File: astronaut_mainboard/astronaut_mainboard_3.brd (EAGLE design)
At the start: 69.5 x 52.1 mm, 23 parts, among them IC1 ADUM1250, IC2 741G3157DBVR, IC3 741G3157DBVR, J10 HF Comm, J6 Ext 5V, J7 UI, J8 Arduino (DWM), J9 GNSS, Q1 BSS138, Q3 BSS138

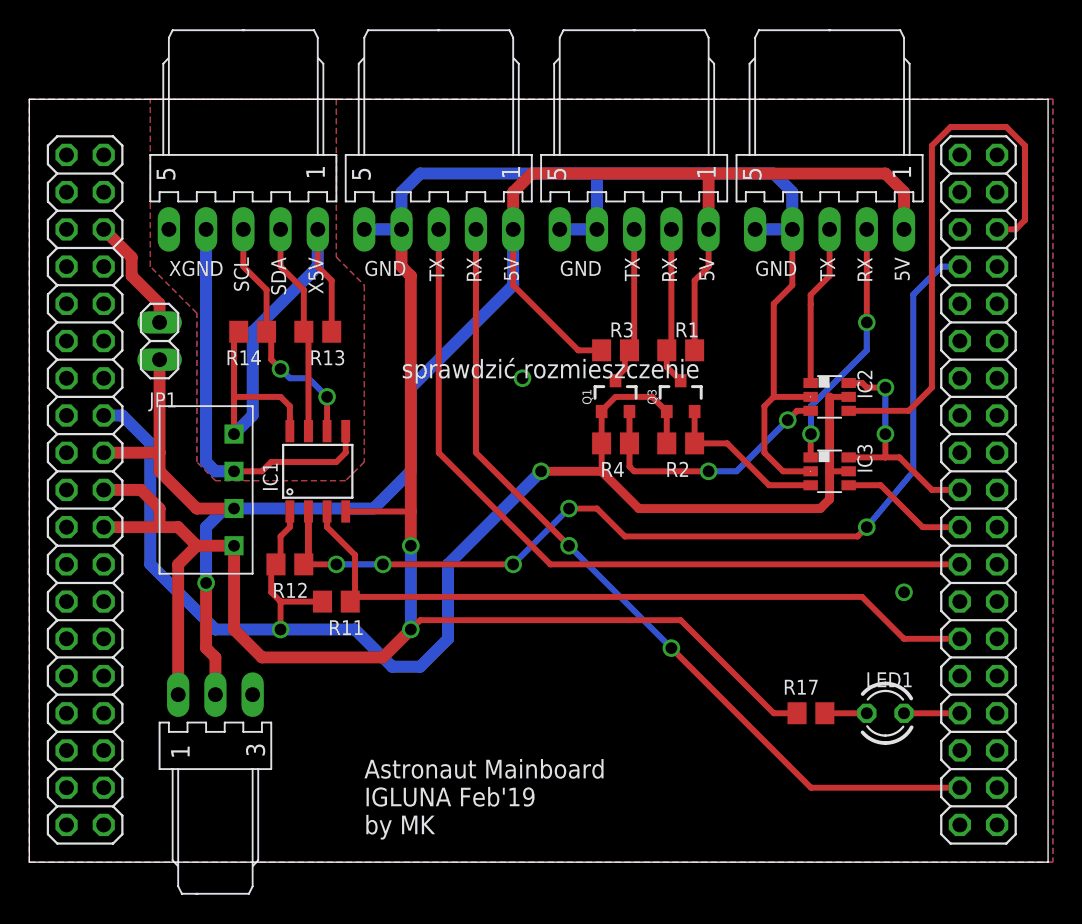
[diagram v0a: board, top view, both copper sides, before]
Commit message: updated lib, corrected boards (after printing)
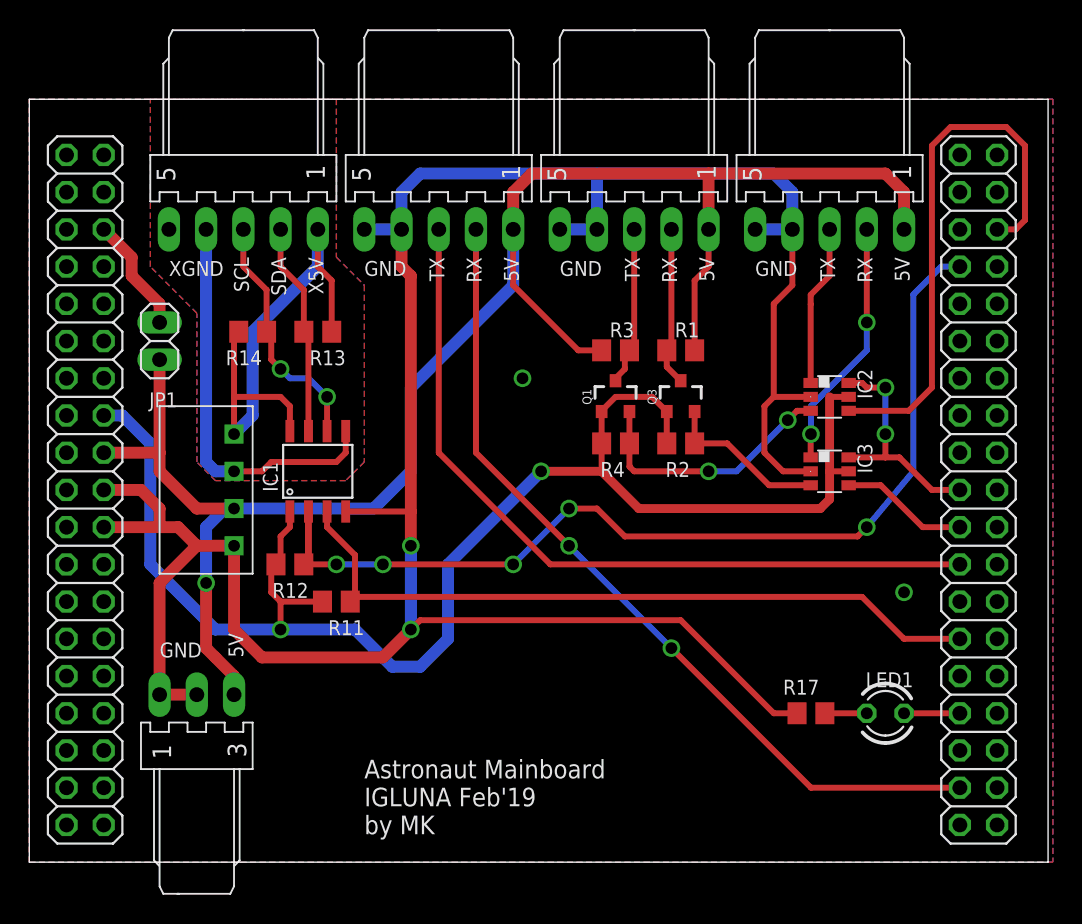
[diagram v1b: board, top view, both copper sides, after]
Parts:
- moved J6 1.27 mm to (12.7, 11.4)
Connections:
- net +5V: no longer J6.2
- net GND: now also J6.2
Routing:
- net GND: track 172.8 -> 175.9 mm
- net +5V: track 121.2 -> 121.7 mm
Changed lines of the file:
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@@
 IGLUNA Feb'19
 by MK</text>
+<text x="15.875" y="13.97" size="1.016" layer="25" rot="R90">5V</text>
+<text x="10.16" y="13.97" size="1.016" layer="25">GND</text>
 </plain>
 <attributes>
@@
 <attribute name="VALUE" x="6.985" y="38.1" size="1.27" layer="27" rot="R270"/>
 </element>
-<element name="J6" library="EP_molex_6410_7395" package="7395-03" value="Ext 5V" x="13.97" y="11.43" smashed="yes" rot="R180">
-<attribute name="VALUE" x="18.6421" y="8.9901" size="1.27" layer="27" ratio="10" rot="R270"/>
+<element name="J6" library="EP_molex_6410_7395" package="7395-03" value="Ext 5V" x="12.7" y="11.43" smashed="yes" rot="R180">
+<attribute name="VALUE" x="17.3721" y="8.9901" size="1.27" layer="27" ratio="10" rot="R270"/>
 </element>
 <element name="J7" library="EP_molex_6410_7395" package="7395-05" value="UI" x="15.875" y="43.18" smashed="yes">
@@
 <contactref element="IC2" pad="2"/>
 <contactref element="R17" pad="1"/>
-<contactref element="U$3" pad="19"/>
-<contactref element="U$3" pad="8"/>
 <contactref element="U$3" pad="20"/>
 <contactref element="U$3" pad="22"/>
-<contactref element="U$3" pad="47"/>
-<contactref element="U$3" pad="58"/>
 <wire x1="6.35" y1="22.86" x2="10.16" y2="22.86" width="0.8128" layer="1"/>
 <wire x1="53.34" y1="43.18" x2="53.34" y2="45.72" width="0.8128" layer="16"/>
@@
 <contactref element="J8" pad="5"/>
 <contactref element="J6" pad="1"/>
-<wire x1="11.43" y1="11.43" x2="11.43" y2="20.32" width="0.8128" layer="1"/>
-<wire x1="11.43" y1="20.32" x2="12.7" y2="21.59" width="0.8128" layer="1"/>
+<wire x1="10.16" y1="11.43" x2="10.16" y2="19.05" width="0.8128" layer="1"/>
+<wire x1="10.16" y1="19.05" x2="12.7" y2="21.59" width="0.8128" layer="1"/>
 <wire x1="26.67" y1="43.18" x2="24.13" y2="43.18" width="0.8128" layer="16"/>
 <wire x1="37.465" y1="43.18" x2="40.005" y2="43.18" width="0.8128" layer="16"/>
@@
 <via x="34.925" y="33.02" extent="1-16" drill="0.8"/>
 <via x="60.96" y="18.415" extent="1-16" drill="0.8"/>
+<contactref element="U$3" pad="19"/>
+<contactref element="U$3" pad="8"/>
+<contactref element="U$3" pad="47"/>
+<contactref element="U$3" pad="58"/>
+<contactref element="J6" pad="2"/>
+<wire x1="10.16" y1="11.43" x2="12.7" y2="11.43" width="0.8128" layer="1"/>
 </signal>
 <signal name="VIN">
@@
 <contactref element="J10" pad="1"/>
 <contactref element="J8" pad="1"/>
-<contactref element="J6" pad="2"/>
 <contactref element="J6" pad="3"/>
 <wire x1="12.7" y1="24.13" x2="10.16" y2="26.67" width="0.8128" layer="1"/>
@@
 <wire x1="13.335" y1="19.05" x2="13.335" y2="14.605" width="0.8128" layer="1"/>
 <wire x1="13.335" y1="14.605" x2="13.97" y2="13.97" width="0.8128" layer="1"/>
-<wire x1="13.97" y1="13.97" x2="13.97" y2="11.43" width="0.8128" layer="1"/>
 <via x="13.335" y="19.05" extent="1-16" drill="0.8"/>
 <wire x1="27.305" y1="32.385" x2="34.29" y2="39.37" width="0.8128" layer="16"/>
 <wire x1="34.29" y1="39.37" x2="34.29" y2="43.18" width="0.8128" layer="16"/>
-<wire x1="13.97" y1="11.43" x2="16.51" y2="11.43" width="0" layer="19" extent="1-1"/>
+<wire x1="13.97" y1="13.97" x2="15.24" y2="12.7" width="0.8128" layer="1"/>
+<wire x1="15.24" y1="12.7" x2="15.24" y2="11.43" width="0.8128" layer="1"/>
 </signal>
 <signal name="VCC">

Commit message: verified, ready to production
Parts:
- LED1: device led:LED3MM -> led:SML1206
- R17: value 470 -> 100
- turned LED1 to 0 degrees
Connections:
- net N$3: now also LED1.C; no longer LED1.K

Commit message: final, after another review
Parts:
- moved JP1 0.63 mm to (9.53, 35.6)
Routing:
- net +5V: track 121.7 -> 120.9 mm

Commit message: really final projects, added gerber files
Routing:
- net GND: vias 4 -> 5
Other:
- board text added: "."
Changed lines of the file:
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@@
 <layer number="19" name="Unrouted" color="6" fill="1" visible="yes" active="yes"/>
 <layer number="20" name="Dimension" color="15" fill="1" visible="yes" active="yes"/>
-<layer number="21" name="tPlace" color="7" fill="1" visible="yes" active="yes"/>
+<layer number="21" name="tPlace" color="7" fill="1" visible="no" active="yes"/>
 <layer number="22" name="bPlace" color="7" fill="1" visible="yes" active="yes"/>
 <layer number="23" name="tOrigins" color="15" fill="1" visible="yes" active="yes"/>
@@
 <layer number="27" name="tValues" color="7" fill="1" visible="yes" active="yes"/>
 <layer number="28" name="bValues" color="7" fill="1" visible="yes" active="yes"/>
-<layer number="29" name="tStop" color="7" fill="3" visible="no" active="yes"/>
-<layer number="30" name="bStop" color="7" fill="6" visible="no" active="yes"/>
-<layer number="31" name="tCream" color="7" fill="4" visible="no" active="yes"/>
-<layer number="32" name="bCream" color="7" fill="5" visible="no" active="yes"/>
-<layer number="33" name="tFinish" color="6" fill="3" visible="no" active="yes"/>
-<layer number="34" name="bFinish" color="6" fill="6" visible="no" active="yes"/>
-<layer number="35" name="tGlue" color="7" fill="4" visible="no" active="yes"/>
-<layer number="36" name="bGlue" color="7" fill="5" visible="no" active="yes"/>
-<layer number="37" name="tTest" color="7" fill="1" visible="no" active="yes"/>
-<layer number="38" name="bTest" color="7" fill="1" visible="no" active="yes"/>
+<layer number="29" name="tStop" color="7" fill="3" visible="yes" active="yes"/>
+<layer number="30" name="bStop" color="7" fill="6" visible="yes" active="yes"/>
+<layer number="31" name="tCream" color="7" fill="4" visible="yes" active="yes"/>
+<layer number="32" name="bCream" color="7" fill="5" visible="yes" active="yes"/>
+<layer number="33" name="tFinish" color="6" fill="3" visible="yes" active="yes"/>
+<layer number="34" name="bFinish" color="6" fill="6" visible="yes" active="yes"/>
+<layer number="35" name="tGlue" color="7" fill="4" visible="yes" active="yes"/>
+<layer number="36" name="bGlue" color="7" fill="5" visible="yes" active="yes"/>
+<layer number="37" name="tTest" color="7" fill="1" visible="yes" active="yes"/>
+<layer number="38" name="bTest" color="7" fill="1" visible="yes" active="yes"/>
 <layer number="39" name="tKeepout" color="4" fill="11" visible="yes" active="yes"/>
 <layer number="40" name="bKeepout" color="1" fill="11" visible="yes" active="yes"/>
@@
 <layer number="42" name="bRestrict" color="1" fill="10" visible="yes" active="yes"/>
 <layer number="43" name="vRestrict" color="2" fill="10" visible="yes" active="yes"/>
-<layer number="44" name="Drills" color="7" fill="1" visible="no" active="yes"/>
-<layer number="45" name="Holes" color="7" fill="1" visible="no" active="yes"/>
-<layer number="46" name="Milling" color="3" fill="1" visible="no" active="yes"/>
-<layer number="47" name="Measures" color="7" fill="1" visible="no" active="yes"/>
+<layer number="44" name="Drills" color="7" fill="1" visible="yes" active="yes"/>
+<layer number="45" name="Holes" color="7" fill="1" visible="yes" active="yes"/>
+<layer number="46" name="Milling" color="3" fill="1" visible="yes" active="yes"/>
+<layer number="47" name="Measures" color="7" fill="1" visible="yes" active="yes"/>
 <layer number="48" name="Document" color="7" fill="1" visible="yes" active="yes"/>
 <layer number="49" name="Reference" color="7" fill="1" visible="yes" active="yes"/>
@@
 <layer number="112" name="tSilk" color="7" fill="1" visible="yes" active="yes"/>
 <layer number="113" name="IDFDebug" color="4" fill="1" visible="yes" active="yes"/>
-<layer number="114" name="Badge_Outline" color="7" fill="1" visible="no" active="yes"/>
-<layer number="115" name="ReferenceISLANDS" color="7" fill="1" visible="no" active="yes"/>
+<layer number="114" name="Badge_Outline" color="7" fill="1" visible="yes" active="yes"/>
+<layer number="115" name="ReferenceISLANDS" color="7" fill="1" visible="yes" active="yes"/>
 <layer number="116" name="Patch_BOT" color="9" fill="4" visible="yes" active="yes"/>
-<layer number="118" name="Rect_Pads" color="7" fill="1" visible="no" active="yes"/>
+<layer number="118" name="Rect_Pads" color="7" fill="1" visible="yes" active="yes"/>
 <layer number="121" name="_tsilk" color="7" fill="1" visible="yes" active="yes"/>
 <layer number="122" name="_bsilk" color="7" fill="1" visible="yes" active="yes"/>
@@
 <text x="15.875" y="13.97" size="1.27" layer="25" font="vector" ratio="15" rot="R90">5V</text>
 <text x="10.16" y="13.97" size="1.27" layer="25" font="vector" ratio="15">GND</text>
+<text x="19.304" y="25.146" size="1.27" layer="25" font="vector" ratio="15" rot="R90">.</text>
+<text x="54.356" y="33.274" size="1.27" layer="25" font="vector" ratio="15" rot="R270">.</text>
+<text x="54.356" y="28.194" size="1.27" layer="25" font="vector" ratio="15" rot="R270">.</text>
+<text x="58.166" y="11.049" size="1.27" layer="25" font="vector" ratio="15" rot="R270">.</text>
 </plain>
 <attributes>
@@
 </class>
 </classes>
-<designrules name="default *">
+<designrules name="jlcpcb_rules">
 <description language="de">&lt;b&gt;EAGLE Design Rules&lt;/b&gt;
 &lt;p&gt;
@@
 <param name="mtCopper" value="0.035mm 0.035mm 0.035mm 0.035mm 0.035mm 0.035mm 0.035mm 0.035mm 0.035mm 0.035mm 0.035mm 0.035mm 0.035mm 0.035mm 0.035mm 0.035mm"/>
 <param name="mtIsolate" value="1.5mm 0.15mm 0.2mm 0.15mm 0.2mm 0.15mm 0.2mm 0.15mm 0.2mm 0.15mm 0.2mm 0.15mm 0.2mm 0.15mm 0.2mm"/>
-<param name="mdWireWire" value="12mil"/>
-<param name="mdWirePad" value="12mil"/>
-<param name="mdWireVia" value="12mil"/>
-<param name="mdPadPad" value="10mil"/>
-<param name="mdPadVia" value="12mil"/>
-<param name="mdViaVia" value="12mil"/>
-<param name="mdSmdPad" value="10mil"/>
-<param name="mdSmdVia" value="10mil"/>
-<param name="mdSmdSmd" value="10mil"/>
-<param name="mdViaViaSameLayer" value="8mil"/>
+<param name="mdWireWire" value="5mil"/>
+<param name="mdWirePad" value="5mil"/>
+<param name="mdWireVia" value="5mil"/>
+<param name="mdPadPad" value="5mil"/>
+<param name="mdPadVia" value="5mil"/>
+<param name="mdViaVia" value="5mil"/>
+<param name="mdSmdPad" value="5mil"/>
+<param name="mdSmdVia" value="5mil"/>
+<param name="mdSmdSmd" value="5mil"/>
+<param name="mdViaViaSameLayer" value="6mil"/>
 <param name="mnLayersViaInSmd" value="2"/>
-<param name="mdCopperDimension" value="20mil"/>
+<param name="mdCopperDimension" value="0.2mm"/>
 <param name="mdDrill" value="12mil"/>
 <param name="mdSmdStop" value="0mil"/>
-<param name="msWidth" value="12mil"/>
-<param name="msDrill" value="24mil"/>
+<param name="msWidth" value="5mil"/>
+<param name="msDrill" value="0.2mm"/>
 <param name="msMicroVia" value="9.99mm"/>
 <param name="msBlindViaRatio" value="0.5"/>
@@
 <param name="rvMicroViaOuter" value="0.25"/>
 <param name="rvMicroViaInner" value="0.25"/>
-<param name="rlMinPadTop" value="10mil"/>
+<param name="rlMinPadTop" value="3mil"/>
 <param name="rlMaxPadTop" value="20mil"/>
 <param name="rlMinPadInner" value="10mil"/>
@@
 <param name="rlMinPadBottom" value="10mil"/>
 <param name="rlMaxPadBottom" value="20mil"/>
-<param name="rlMinViaOuter" value="8mil"/>
+<param name="rlMinViaOuter" value="3mil"/>
 <param name="rlMaxViaOuter" value="20mil"/>
 <param name="rlMinViaInner" value="8mil"/>
@@
 <param name="srMinRoundness" value="0mil"/>
 <param name="srMaxRoundness" value="0mil"/>
-<param name="slThermalIsolate" value="12mil"/>
+<param name="slThermalIsolate" value="10mil"/>
 <param name="slThermalsForVias" value="0"/>
 <param name="dpMaxLengthDifference" value="10mm"/>
@@
 <contactref element="J6" pad="2"/>
 <wire x1="10.16" y1="11.43" x2="12.7" y2="11.43" width="0.8128" layer="1"/>
+<via x="11.43" y="21.59" extent="1-16" drill="0.8"/>
 </signal>
 <signal name="VIN">

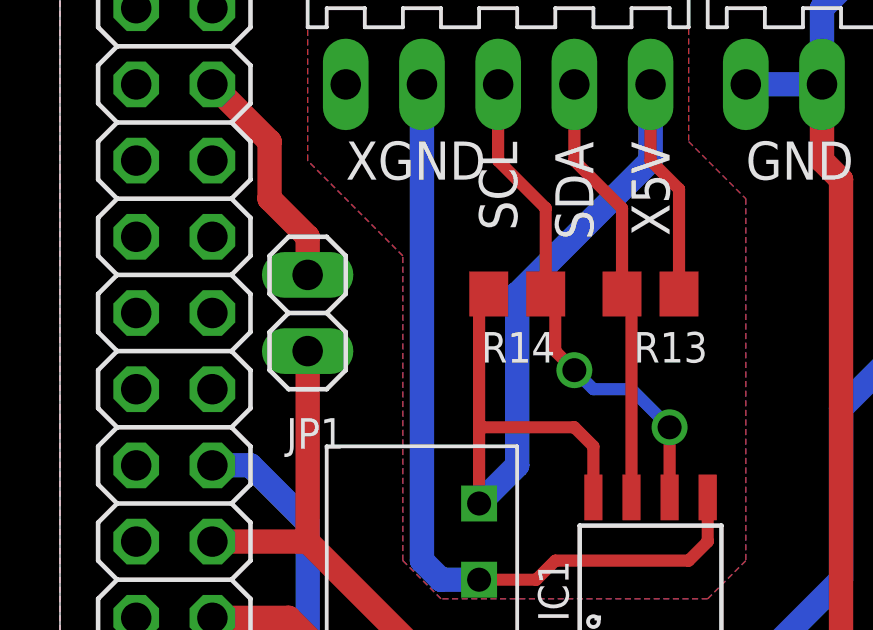
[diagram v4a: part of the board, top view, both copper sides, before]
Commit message: corrected gerbers, cleaned schematics, added documnetation
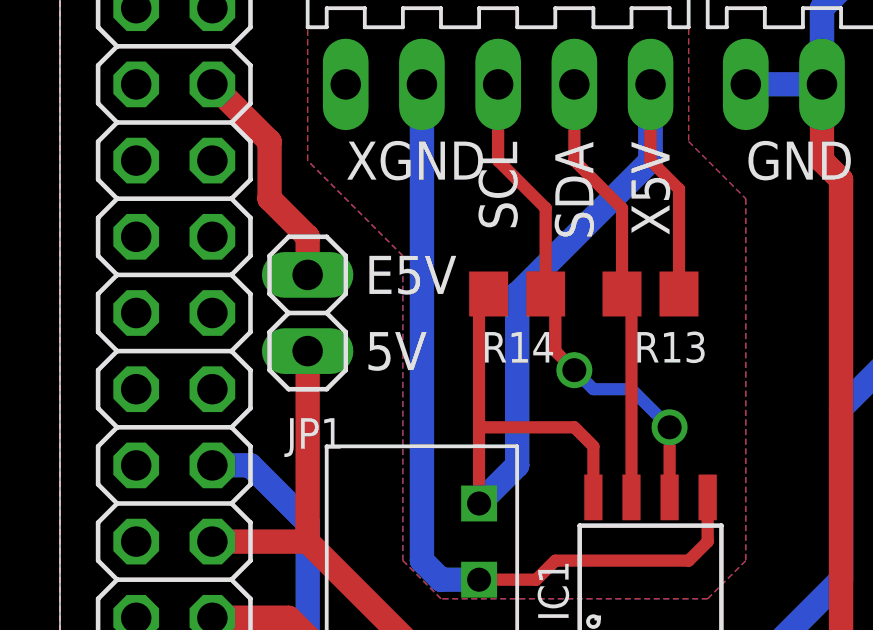
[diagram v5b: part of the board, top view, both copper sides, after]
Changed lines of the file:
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@@
 <wire x1="70.79" y1="52.06" x2="1.27" y2="52.06" width="0" layer="20"/>
 <wire x1="1.27" y1="52.06" x2="1.27" y2="0" width="0" layer="20"/>
-<text x="11.43" y="33.655" size="1.27" layer="26" font="vector" ratio="15">5V</text>
-<text x="11.43" y="36.195" size="1.27" layer="26" font="vector" ratio="15">E5V</text>
+<text x="11.43" y="33.655" size="1.27" layer="25" font="vector" ratio="15">5V</text>
+<text x="11.43" y="36.195" size="1.27" layer="25" font="vector" ratio="15">E5V</text>
 <text x="57.785" y="41.275" size="1.27" layer="25" font="vector" ratio="15" rot="R270">RX</text>
 <text x="44.45" y="41.275" size="1.27" layer="25" font="vector" ratio="15" rot="R270">RX</text>
